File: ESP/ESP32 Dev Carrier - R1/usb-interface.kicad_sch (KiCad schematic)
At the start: 18 parts, among them J2 USB_B_Micro, Q1 MMS9013, Q2 MMS9013, U4 CP2102N-Axx-xQFN28

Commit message: Blurgh. Almost ready to order.
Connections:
- net +3V3: now also D3.2 (A), D4.2 (A); no longer R13.2, R16.2
- net at D3.1 (K): now also R13.2; no longer U4.19 (~{TXT}/GPIO.0)
- net at R13.1: now also U4.19 (~{TXT}/GPIO.0); no longer D3.2 (A)
- net at R16.1: now also U4.18 (~{RXT}/GPIO.1); no longer D4.2 (A)
- net at D4.1 (K): now also R16.2; no longer U4.18 (~{RXT}/GPIO.1)
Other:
- moved on the sheet: D3, D4, R13, R16
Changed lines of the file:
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@@
     (stroke (width 0) (type default) (color 0 0 0 0))
   )
-  (wire (pts (xy 144.78 81.28) (xy 144.78 78.74))
+  (wire (pts (xy 144.78 83.82) (xy 144.78 81.28))
     (stroke (width 0) (type default) (color 0 0 0 0))
   )
@@
     (stroke (width 0) (type default) (color 0 0 0 0))
   )
-  (wire (pts (xy 137.16 78.74) (xy 137.16 81.28))
+  (wire (pts (xy 137.16 81.28) (xy 137.16 83.82))
     (stroke (width 0) (type default) (color 0 0 0 0))
   )
@@
     (pin "2")
   )
-  (symbol (lib_id "Device:LED") (at 137.16 85.09 90) (unit 1)
-    (in_bom yes) (on_board yes)
-    (property "Reference" "D3" (id 0) (at 140.1572 84.0994 90)
+  (symbol (lib_id "Device:LED") (at 137.16 77.47 90) (unit 1)
+    (in_bom yes) (on_board yes)
+    (property "Reference" "D3" (id 0) (at 140.1572 76.4794 90)
       (effects (font (size 1.27 1.27)) (justify right))
     )
-    (property "Value" "LED" (id 1) (at 140.1572 86.4108 90)
+    (property "Value" "LED" (id 1) (at 140.1572 78.7908 90)
       (effects (font (size 1.27 1.27)) (justify right))
     )
-    (property "Footprint" "custom:CHIPLED_0603" (id 2) (at 137.16 85.09 0)
-      (effects (font (size 1.27 1.27)) hide)
-    )
-    (property "Datasheet" "~" (id 3) (at 137.16 85.09 0)
-      (effects (font (size 1.27 1.27)) hide)
-    )
-    (property "LCSC" "C14663" (id 4) (at 140.1572 84.0994 0)
+    (property "Footprint" "custom:CHIPLED_0603" (id 2) (at 137.16 77.47 0)
+      (effects (font (size 1.27 1.27)) hide)
+    )
+    (property "Datasheet" "~" (id 3) (at 137.16 77.47 0)
+      (effects (font (size 1.27 1.27)) hide)
+    )
+    (property "LCSC" "C14663" (id 4) (at 140.1572 76.4794 0)
       (effects (font (size 1.27 1.27)) hide)
     )
@@
     (pin "3")
   )
-  (symbol (lib_id "Device:R_Small") (at 144.78 76.2 180) (unit 1)
-    (in_bom yes) (on_board yes)
-    (property "Reference" "R16" (id 0) (at 149.86 76.2 90))
-    (property "Value" "470R" (id 1) (at 147.32 76.2 90))
-    (property "Footprint" "Resistor_SMD:R_0603_1608Metric" (id 2) (at 144.78 76.2 0)
-      (effects (font (size 1.27 1.27)) hide)
-    )
-    (property "Datasheet" "~" (id 3) (at 144.78 76.2 0)
-      (effects (font (size 1.27 1.27)) hide)
-    )
-    (property "LCSC" "C14663" (id 4) (at 149.86 76.2 0)
+  (symbol (lib_id "Device:R_Small") (at 144.78 86.36 180) (unit 1)
+    (in_bom yes) (on_board yes)
+    (property "Reference" "R16" (id 0) (at 149.86 86.36 90))
+    (property "Value" "470R" (id 1) (at 147.32 86.36 90))
+    (property "Footprint" "Resistor_SMD:R_0603_1608Metric" (id 2) (at 144.78 86.36 0)
+      (effects (font (size 1.27 1.27)) hide)
+    )
+    (property "Datasheet" "~" (id 3) (at 144.78 86.36 0)
+      (effects (font (size 1.27 1.27)) hide)
+    )
+    (property "LCSC" "C14663" (id 4) (at 149.86 86.36 0)
       (effects (font (size 1.27 1.27)) hide)
     )
@@
     (pin "3")
   )
-  (symbol (lib_id "Device:LED") (at 144.78 85.09 90) (unit 1)
-    (in_bom yes) (on_board yes)
-    (property "Reference" "D4" (id 0) (at 147.7772 84.0994 90)
+  (symbol (lib_id "Device:LED") (at 144.78 77.47 90) (unit 1)
+    (in_bom yes) (on_board yes)
+    (property "Reference" "D4" (id 0) (at 147.7772 76.4794 90)
       (effects (font (size 1.27 1.27)) (justify right))
     )
-    (property "Value" "LED" (id 1) (at 147.7772 86.4108 90)
+    (property "Value" "LED" (id 1) (at 147.7772 78.7908 90)
       (effects (font (size 1.27 1.27)) (justify right))
     )
-    (property "Footprint" "custom:CHIPLED_0603" (id 2) (at 144.78 85.09 0)
-      (effects (font (size 1.27 1.27)) hide)
-    )
-    (property "Datasheet" "~" (id 3) (at 144.78 85.09 0)
-      (effects (font (size 1.27 1.27)) hide)
-    )
-    (property "LCSC" "C14663" (id 4) (at 147.7772 84.0994 0)
+    (property "Footprint" "custom:CHIPLED_0603" (id 2) (at 144.78 77.47 0)
+      (effects (font (size 1.27 1.27)) hide)
+    )
+    (property "Datasheet" "~" (id 3) (at 144.78 77.47 0)
+      (effects (font (size 1.27 1.27)) hide)
+    )
+    (property "LCSC" "C14663" (id 4) (at 147.7772 76.4794 0)
       (effects (font (size 1.27 1.27)) hide)
     )
@@
     (pin "1")
   )
-  (symbol (lib_id "Device:R_Small") (at 137.16 76.2 180) (unit 1)
-    (in_bom yes) (on_board yes)
-    (property "Reference" "R13" (id 0) (at 138.6586 75.0316 0)
+  (symbol (lib_id "Device:R_Small") (at 137.16 86.36 180) (unit 1)
+    (in_bom yes) (on_board yes)
+    (property "Reference" "R13" (id 0) (at 138.6586 85.1916 0)
       (effects (font (size 1.27 1.27)) (justify right))
     )
-    (property "Value" "470R" (id 1) (at 138.6586 77.343 0)
+    (property "Value" "470R" (id 1) (at 138.6586 87.503 0)
       (effects (font (size 1.27 1.27)) (justify right))
     )
-    (property "Footprint" "Resistor_SMD:R_0603_1608Metric" (id 2) (at 137.16 76.2 0)
-      (effects (font (size 1.27 1.27)) hide)
-    )
-    (property "Datasheet" "~" (id 3) (at 137.16 76.2 0)
-      (effects (font (size 1.27 1.27)) hide)
-    )
-    (property "LCSC" "C14663" (id 4) (at 138.6586 75.0316 0)
-      (effects (font (size 1.27 1.27)) hide)
-    )
+    (property "Footprint" "Resistor_SMD:R_0603_1608Metric" (id 2) (at 137.16 86.36 0)
+      (effects (font (size 1.27 1.27)) hide)
+    )
+    (property "Datasheet" "~" (id 3) (at 137.16 86.36 0)
+      (effects (font (size 1.27 1.27)) hide)
+    )
+    (property "LCSC" "C14663" (id 4) (at 138.6586 85.1916 0)
+      (effects (font (size 1.27 1.27)) hide)
+    )

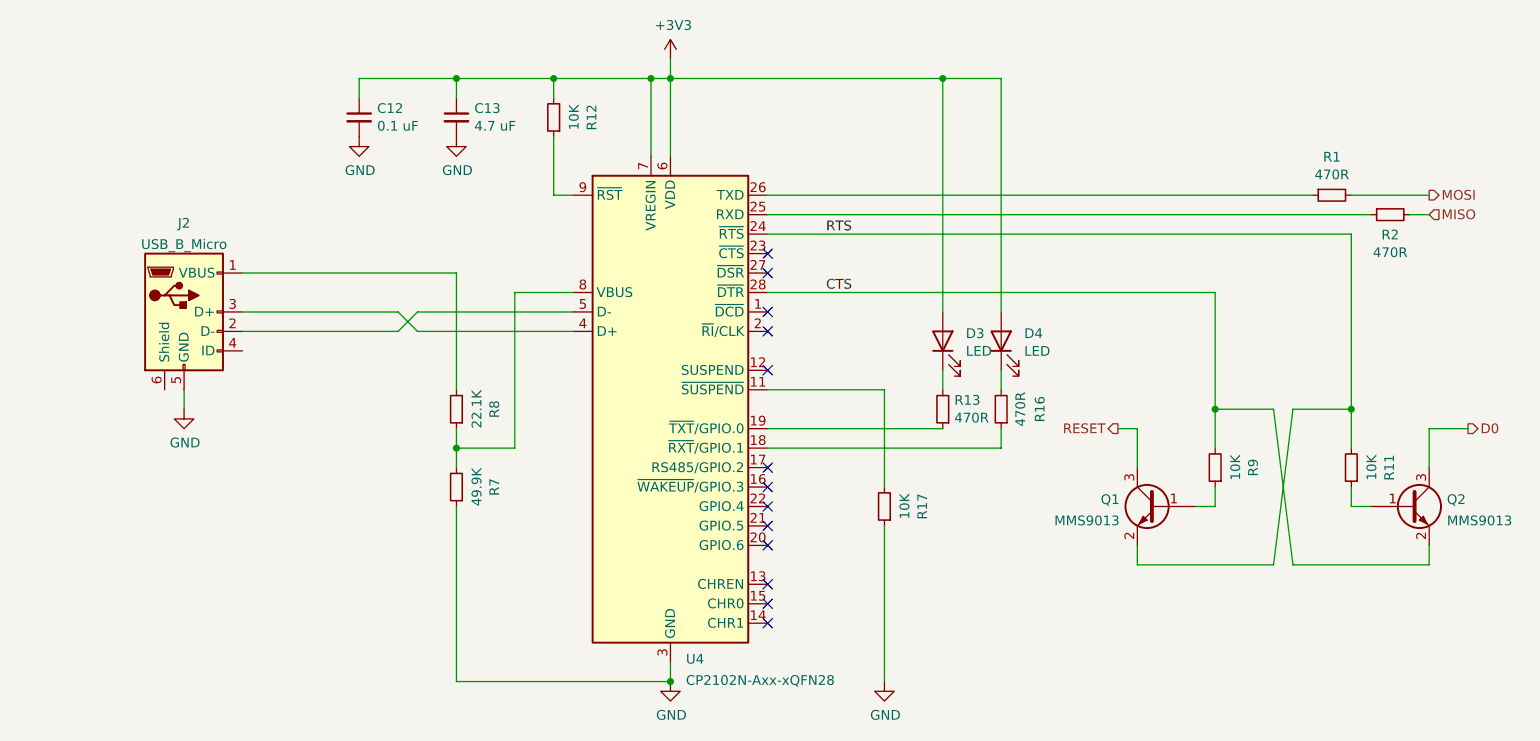
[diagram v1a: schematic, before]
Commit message: Reworking things to use the new controller PCB.
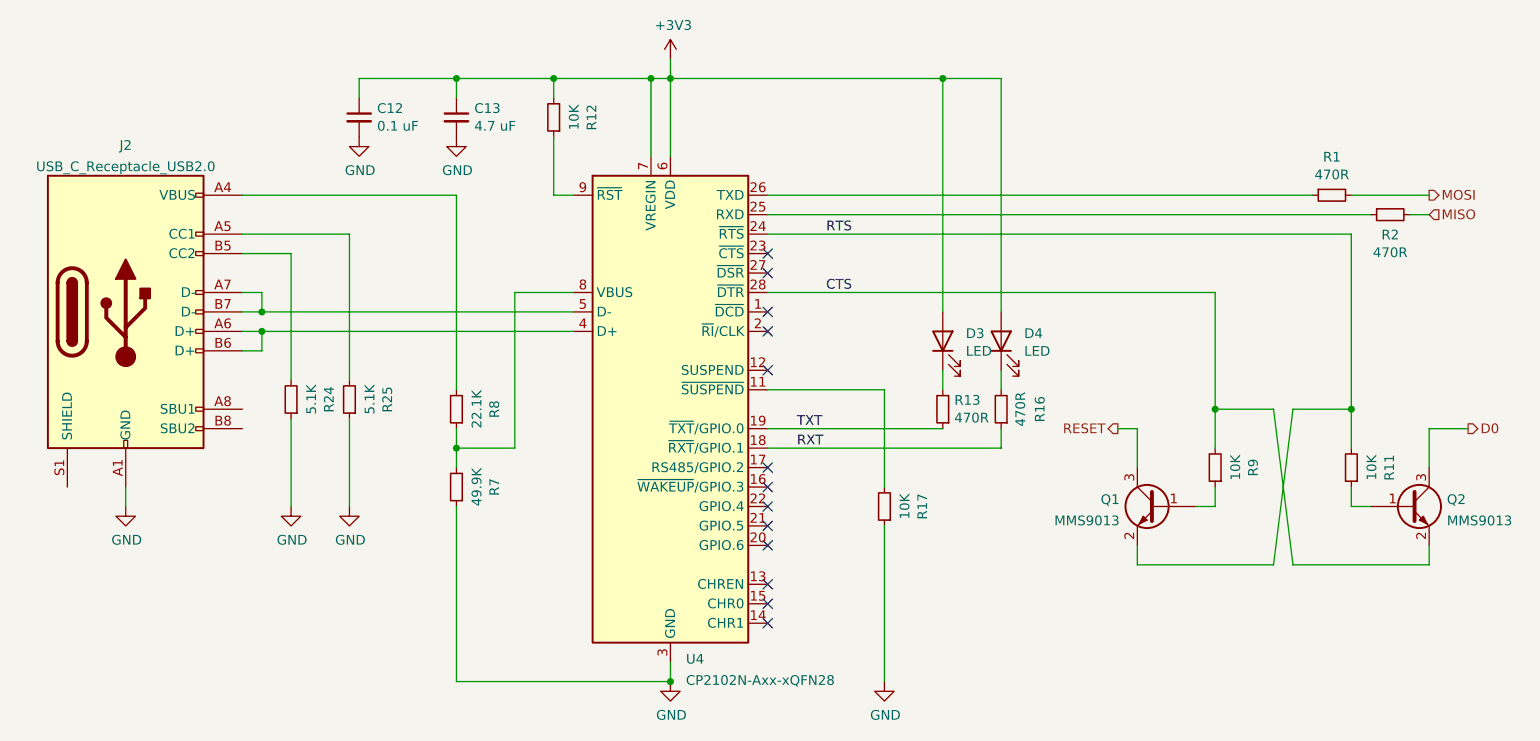
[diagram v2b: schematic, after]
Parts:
- removed J2: USB_B_Micro, custom:Molex--0-0-0, symbol Connector:USB_B_Micro
- added J2: USB_C_Receptacle_USB2.0, Connector_USB:USB_C_Receptacle_Amphenol_12401610E4-2A, symbol Connector:USB_C_Receptacle_USB2.0
- added R24, R25: 5.1K, Resistor_SMD:R_0603_1608Metric, symbol Device:R_Small
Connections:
- net GND: now also J2.A1 (GND), J2.A12 (GND), J2.B1 (GND), J2.B12 (GND), R24.1, R25.1
- net at R8.2: now also J2.A4 (VBUS), J2.A9 (VBUS), J2.B4 (VBUS), J2.B9 (VBUS)
- net at U4.5 (D-): now also J2.A7 (D-), J2.B7 (D-)
- net at U4.4 (D+): now also J2.A6 (D+), J2.B6 (D+)
- net RXT: now reaches R16.1, U4.18 (~{RXT}/GPIO.1)
- net TXT: now reaches R13.1, U4.19 (~{TXT}/GPIO.0)
- new net: J2.B5 (CC2), R24.2
- new net: J2.A5 (CC1), R25.2
